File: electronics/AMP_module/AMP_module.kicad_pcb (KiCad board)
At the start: 2 copper layers, 19 x 34 mm, 8 parts, among them J1 1, J2 2, J3 3, J4 4, J5 5, J6 6

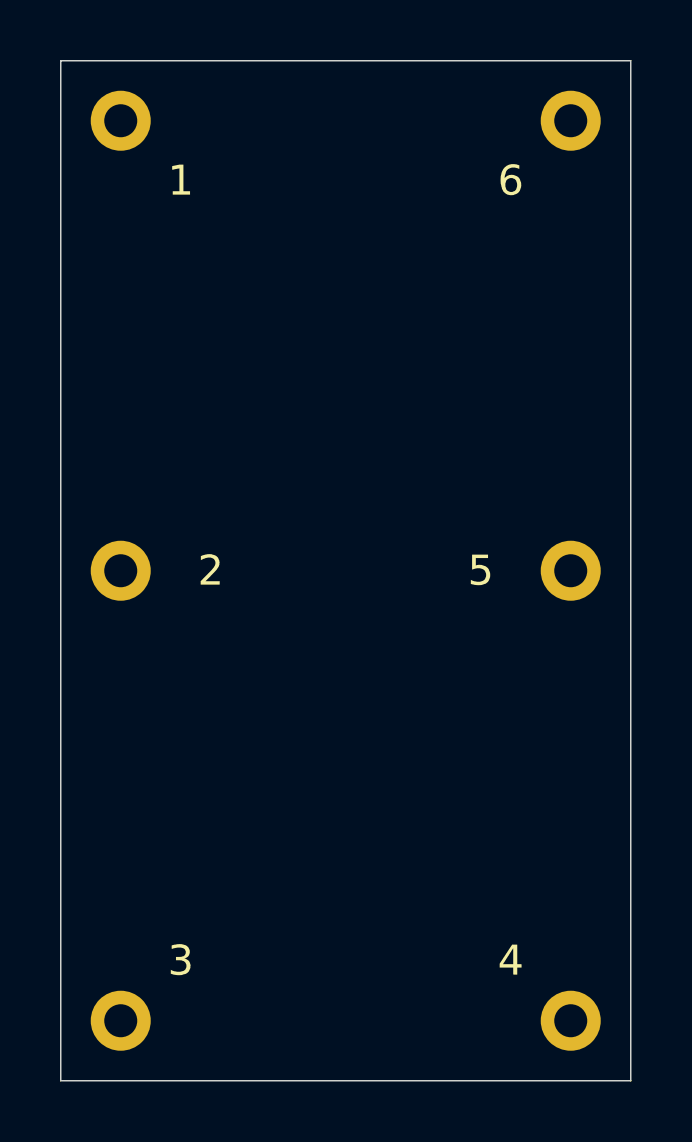
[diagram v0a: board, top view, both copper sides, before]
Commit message: added more cap footprints
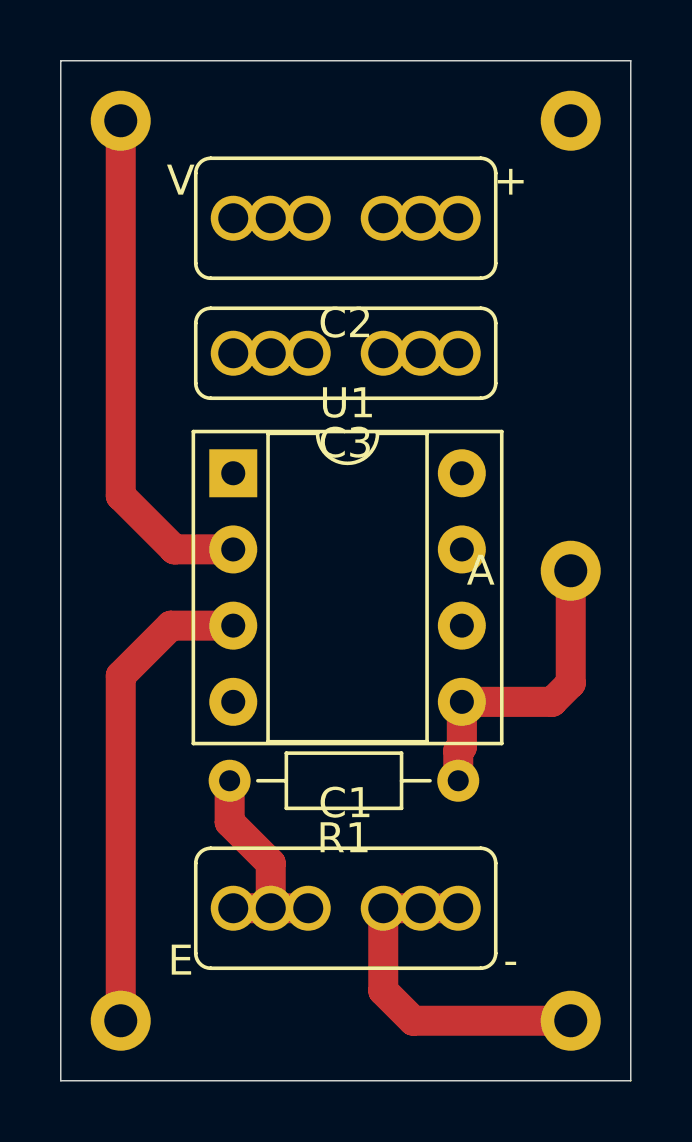
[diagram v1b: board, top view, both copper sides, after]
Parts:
- removed J2: 2, mill-max:PC_pin_nail_head_6092
- added C1: 330n, SquantorRcl:C-025_050_075-040X100, F.Cu at (149.5, 89.2)
- added C2: 330n, SquantorRcl:C-025_050_075-040X100, F.Cu at (149.5, 66.2)
- added C3: 330p, SquantorRcl:C-025_050_075-030X100, F.Cu at (149.5, 70.8)
- added R1: R, Resistor_THT:R_Axial_DIN0204_L3.6mm_D1.6mm_P7.62mm_Horizontal, F.Cu at (153.2, 85.0)
- added U1: TBA820M, Package_DIP:DIP-8_W7.62mm_Socket, F.Cu at (145.8, 74.8)
- J1: value 1 -> V
- J3: value 3 -> E
- J4: value 4 -> -
- J5: value 5 -> A
- J6: value 6 -> +
- N1: value 20201120 -> V20201120
- moved N1 0.35 mm to (148.8, 82.2)
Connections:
- J3 pad 1: Net-(J1-Pad1) -> Net-(J3-Pad1)
- J4 pad 1: Net-(J1-Pad1) -> Net-(C1-Pad2)
- J5 pad 1: Net-(J1-Pad1) -> Net-(C3-Pad1)
- J6 pad 1: Net-(J1-Pad1) -> Net-(C2-Pad1)
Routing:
- net Net-(J1-Pad1): track 0.00 -> 17.0 mm
- net Net-(J3-Pad1): track 0.00 -> 15.9 mm
- net Net-(C1-Pad2): track 0.00 -> 11.9 mm
- net Net-(C3-Pad1): track 0.00 -> 10.3 mm
- net Net-(C1-Pad1): track 0.00 -> 7.32 mm

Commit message: updated footprints and values, but also ripped up all traces, they need to be on the bottom
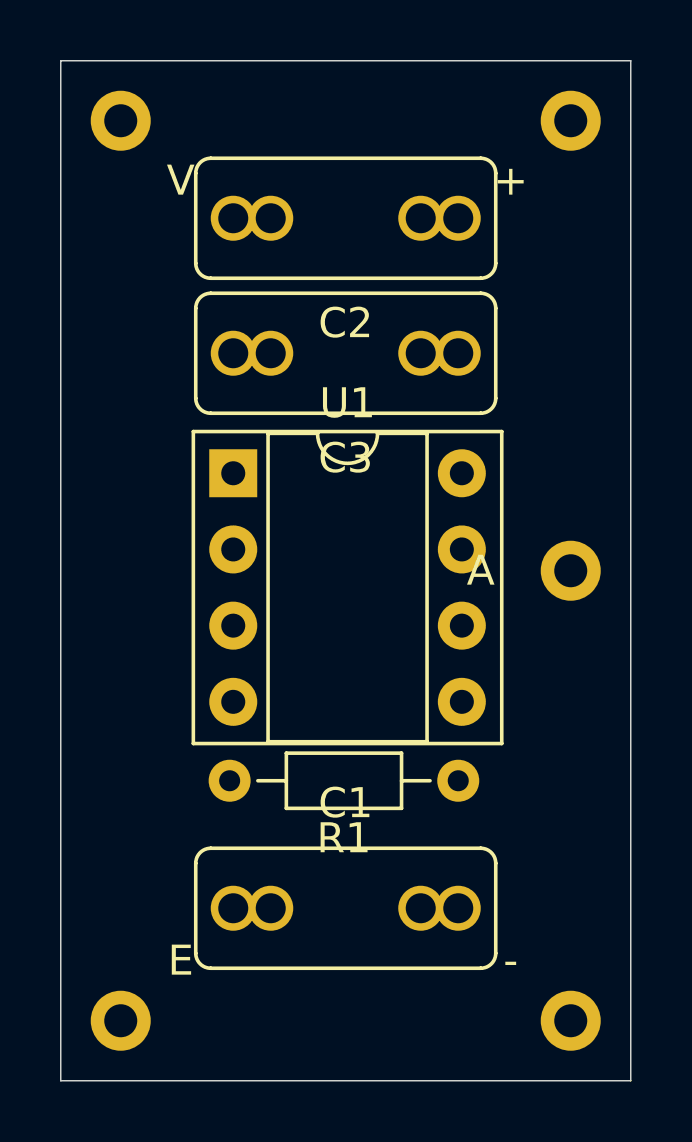
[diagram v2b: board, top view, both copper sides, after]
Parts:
- C1, C2: footprint SquantorRcl:C-025_050_075-040X100 -> SquantorRcl:C-050_075-040X100
- C3: footprint SquantorRcl:C-025_050_075-030X100 -> SquantorRcl:C-050_075-040X100
- N1: value V20201120 -> V20201125
- R1: value R -> 1
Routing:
- net Net-(J1-Pad1): track 17.0 -> 0.00 mm
- net Net-(J3-Pad1): track 15.9 -> 0.00 mm
- net Net-(C1-Pad2): track 11.9 -> 0.00 mm
- net Net-(C3-Pad1): track 10.3 -> 0.00 mm
- net Net-(C1-Pad1): track 7.32 -> 0.00 mm
